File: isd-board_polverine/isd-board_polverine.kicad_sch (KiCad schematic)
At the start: 30 parts, among them J10 Conn_01x08, J11 Conn_01x08, J12 5035661302, J2 Conn_01x04_Socket, J4 Conn_02x08_Odd_Even, J5 Conn_02x08_Odd_Even, J6 Conn_01x05_Socket, J7 Conn_01x08, J8 USB_C_Receptacle_PowerOnly_6P, J9 Conn_01x04_Socket, Q1 DMG9926UDM, U1 DW01A

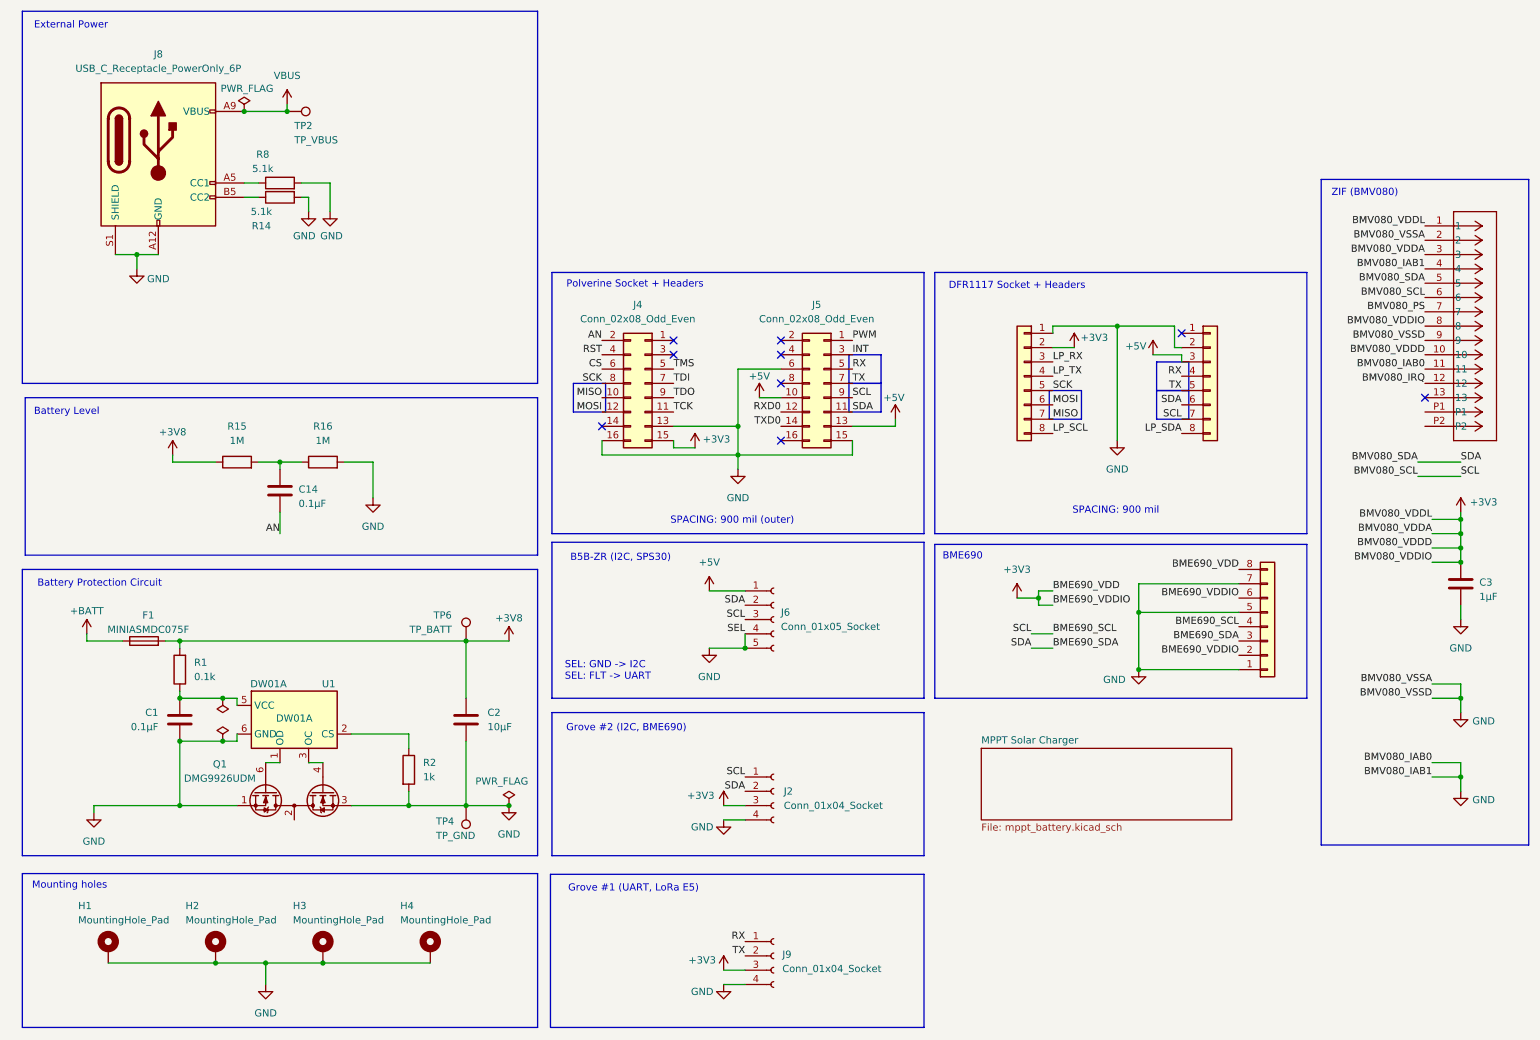
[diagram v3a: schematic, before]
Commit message: update: sch/pcb (pin routing, bmv690/bmv080 footprints, power switch ic)
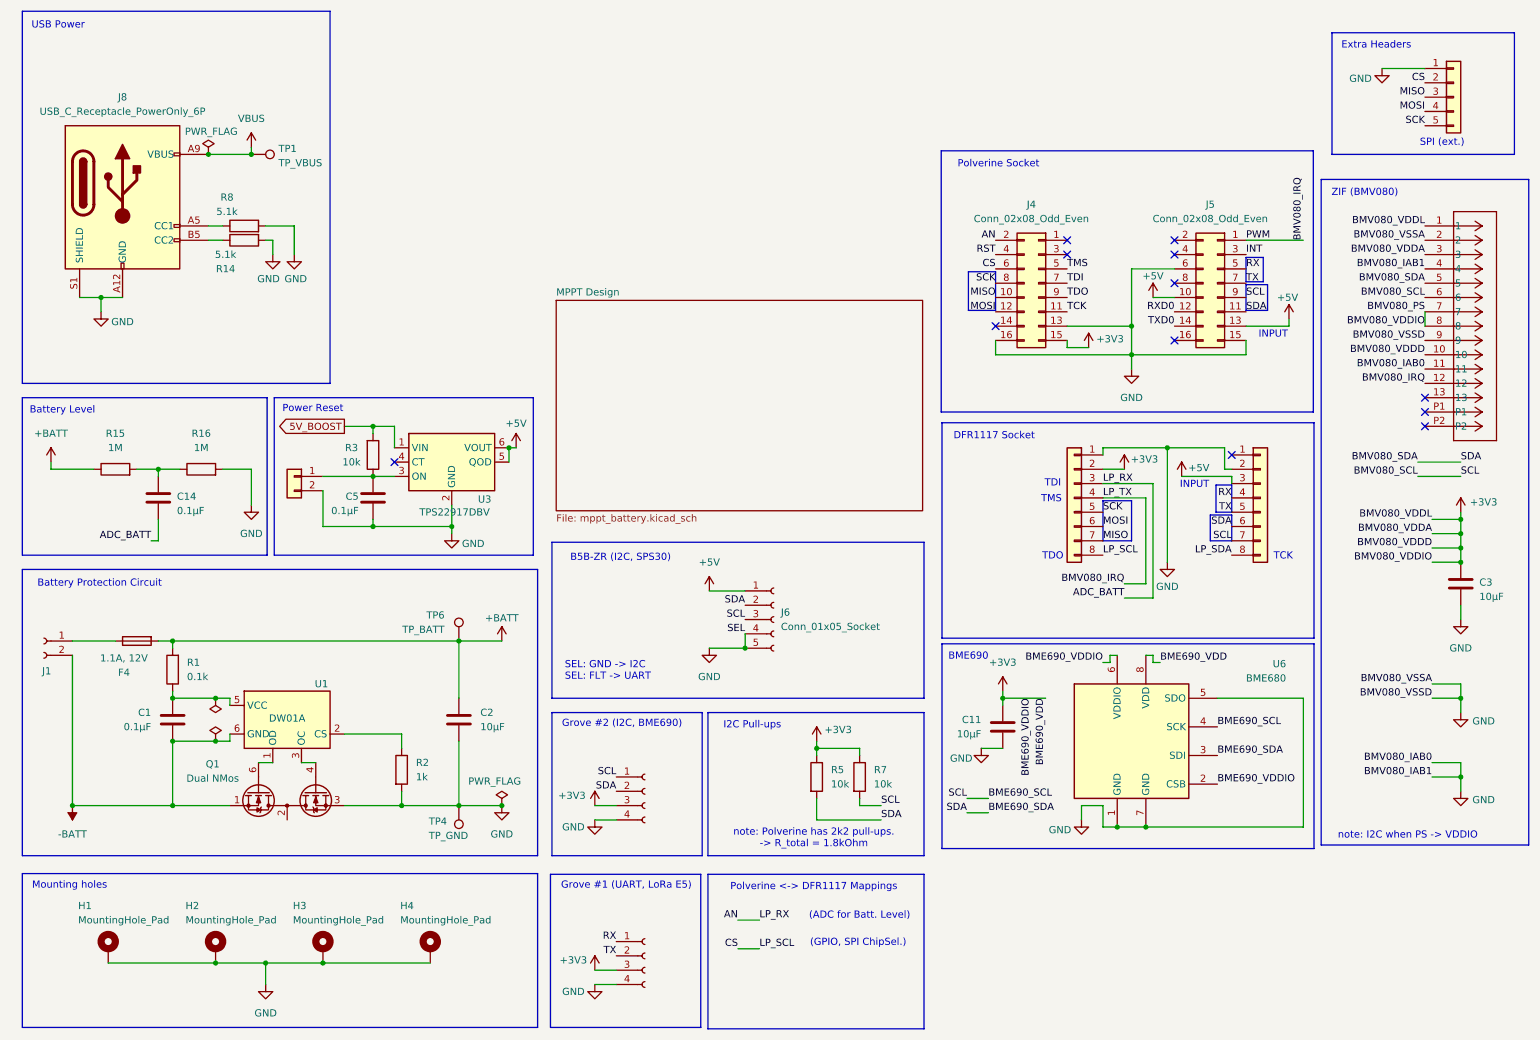
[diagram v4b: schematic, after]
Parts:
- removed F1: MINIASMDC075F, Fuse:Fuse_1812_4532Metric_Pad1.30x3.40mm_HandSolder, symbol Device:Fuse
- removed J11: Conn_01x08, Package_LGA:Bosch_LGA-8_3x3mm_P0.8mm_ClockwisePinNumbering, symbol Connector_Generic:Conn_01x08
- removed TP2: TP_VBUS, TestPoint:TestPoint_Pad_D2.5mm, symbol Connector:TestPoint
- added C11: 10µF, Capacitor_SMD:C_0805_2012Metric_Pad1.18x1.45mm_HandSolder, symbol Device:C
- added C5: 0.1µF, Capacitor_SMD:C_0805_2012Metric_Pad1.18x1.45mm_HandSolder, symbol Device:C
- added F4: 1.1A, 12V, Fuse:Fuse_1210_3225Metric_Pad1.42x2.65mm_HandSolder, symbol Device:Fuse
- added J1: Conn_01x02_Socket, Connector_JST:JST_PH_S2B-PH-K_1x02_P2.00mm_Horizontal, symbol Connector:Conn_01x02_Socket
- added J13: Conn_01x05, Connector_PinHeader_2.54mm:PinHeader_1x05_P2.54mm_Vertical, symbol Connector_Generic:Conn_01x05
- added J16: Conn_01x02, Connector_PinHeader_2.54mm:PinHeader_1x02_P2.54mm_Vertical, symbol Connector_Generic:Conn_01x02
- added R3, R5, R7: 10k, Resistor_SMD:R_0805_2012Metric_Pad1.20x1.40mm_HandSolder, symbol Device:R
- added TP1: TP_VBUS, TestPoint:TestPoint_Pad_1.5x1.5mm, symbol Connector:TestPoint
- added U3: TPS22917DBV, Package_TO_SOT_SMD:SOT-23-6_Handsoldering, symbol Power_Management:TPS22917DBV
- added U6: BME680, Package_LGA:Bosch_LGA-8_3x3mm_P0.8mm_ClockwisePinNumbering, symbol Sensor:BME680
- C1, C14: MPN (none) -> 399-C0805C104K5RACTUCT-ND
- C2: MPN (none) -> GRM21BR61E106KA73K
- C3: value 1µF -> 10µF; MPN (none) -> GRM21BR61E106KA73K
- H1, H2, H3, H4: MPN (none) -> none
- J10, J7: MPN (none) -> PPTC081LFBN-RC
- J12: footprint CON_5035661302_MOL -> footprint:CON_5035661302_MOL; MPN (none) -> 046844713002846+
- J2, J9: MPN (none) -> 1597-1082-ND
- J4, J5: MPN (none) -> 732-61301621821-ND
- J6: MPN (none) -> B5B-ZR
- J8: MPN (none) -> USB4125-GF-A
- Q1: value DMG9926UDM -> Dual NMos; MPN (none) -> DMG9926UDMDICT-ND
- R1: MPN (none) -> 541-100CCT-ND
- R14, R8: MPN (none) -> 311-5.1KARCT-ND
- R15, R16: MPN (none) -> 408-RG2012P-105-B-T5CT-ND
- R2: MPN (none) -> 10-ERJ-HP6J102VCT-ND
- TP4: footprint TestPoint:TestPoint_Pad_D2.5mm -> TestPoint:TestPoint_Pad_D1.0mm; MPN (none) -> none; now left out of the parts list
- TP6: footprint TestPoint:TestPoint_Pad_D2.5mm -> TestPoint:TestPoint_Pad_1.5x1.5mm; MPN (none) -> none; now left out of the parts list
- U1: MPN (none) -> DW01A; MPU DW01A -> (none)
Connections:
- net +3V8 is gone; now on net +BATT: C2.1, R1.2, R15.1, TP6.1
- net BMV080_PS is gone; now on net +3V3: J12.7
- net LP_RX is gone; now on net ADC_BATT: J10.3 (Pin_3)
- net LP_SCL is gone; now on net CS: J10.8 (Pin_8)
- net LP_TX is gone; now on net BMV080_IRQ: J10.4 (Pin_4)
- net PWM is gone; now on net BMV080_IRQ: J5.1 (Pin_1)
- net +3V3: now also C11.1, R5.1, R7.1, U6.2 (CSB), U6.6 (VDDIO), U6.8 (VDD)
- net +5V: now also U3.5 (QOD), U3.6 (VOUT)
- net +BATT: now also F4.2
- net BME690_SCL: now also R7.2, U6.4 (SCK)
- net BME690_SDA: now also R5.2, U6.3 (SDI)
- net CS: now also J13.2 (Pin_2)
- net GND: now also C11.2, C5.2, J13.1 (Pin_1), J16.2 (Pin_2), U3.2 (GND), U6.1 (GND), U6.5 (SDO), U6.7 (GND); no longer C1.2, Q1.1 (D1), U1.6 (GND)
- net MISO: now also J13.3 (Pin_3)
- net MOSI: now also J13.4 (Pin_4)
- net SCK: now also J13.5 (Pin_5)
- net VBUS: now also TP1.1
- net AN renamed ADC_BATT
- new net: C5.1, J16.1 (Pin_1), R3.1, U3.3 (ON)
- new net: F4.1, J1.1 (Pin_1)
- new net -BATT: C1.2, J1.2 (Pin_2), Q1.1 (D1), U1.6 (GND)
- new net 5V_BOOST: R3.2, U3.1 (VIN)
- no-connect marks 9 -> 12
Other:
- removed sheet MPPT Solar Charger
- added sheet MPPT Design (mppt_battery.kicad_sch)
- note added: "(ADC for Batt. Level)"
- note added: "(GPIO, SPI ChipSel.)"
- note added: "DFR1117 Socket"
- note added: "Extra Headers"
- note added: "I2C Pull-ups"
- note added: "INPUT"
- note added: "Polverine <-> DFR1117 Mappings"
- note added: "Polverine Socket"
- note added: "Power Reset"
- note added: "SPI (ext.)"
- note added: "TCK"
- note added: "TDI"
- note added: "TDO"
- note added: "TMS"
- note added: "USB Power"
- note added: "note: I2C when PS -> VDDIO"
- note added: "note: Polverine has 2k2 pull-ups. -> R_total = 1.8kOhm"
- note removed: "DFR1117 Socket + Headers"
- note removed: "External Power"
- note removed: "Polverine Socket + Headers"
- note removed: "SPACING: 900 mil"
- note removed: "SPACING: 900 mil (outer)"
- title: Polverine Carrier Board -> ISD Prototype Board (Dual-Socket)
- moved on the sheet: C1, C14, C2, J4, J5, J8, Q1, R1, R14, R15, R16, R2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
